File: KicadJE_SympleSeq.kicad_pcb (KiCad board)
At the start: 2 copper layers, 80 x 100 mm, 75 parts, among them J101 CV-Out, J102 Reset + Step, J103 CV-G8_Mod1, J104 CV-G8_Mod2, J105 Clk_Hold, J106 G8-Out, J107 Reset + Step 1-4, J108 Reset + Step 5-8, J109 CV-G8_Base, J201 clk_in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

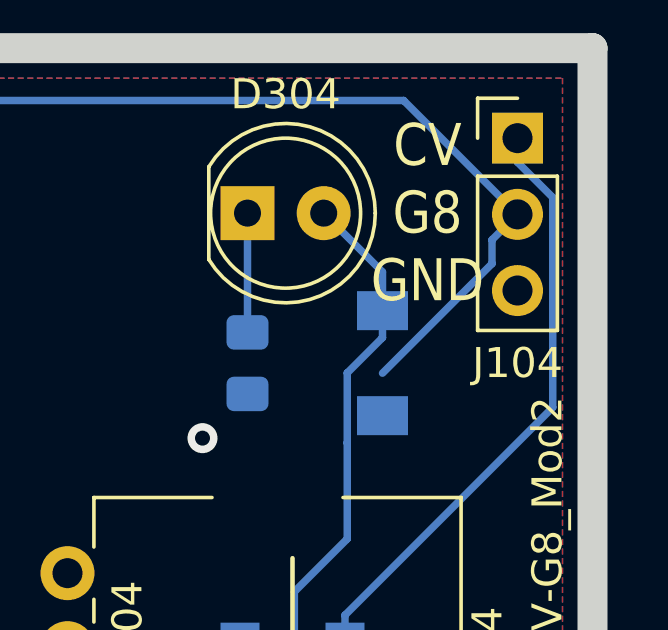
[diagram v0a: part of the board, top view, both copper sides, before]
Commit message: D310 connected
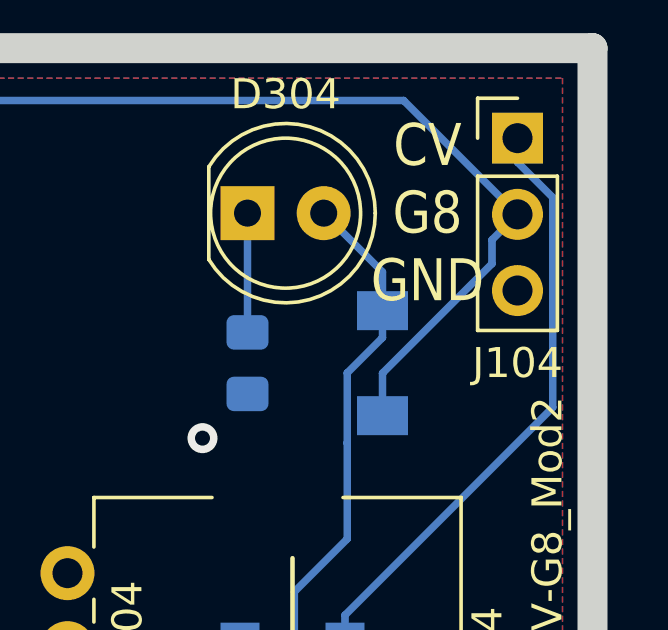
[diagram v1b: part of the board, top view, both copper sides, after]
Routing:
- net G8_M: track 166.9 -> 168.3 mm
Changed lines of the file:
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@@
-(kicad_pcb (version 20171130) (host pcbnew "(5.1.0)-1")
+(kicad_pcb (version 20171130) (host pcbnew "(5.1.5)-3")
   (general
     (thickness 1.6)
     (drawings 22)
-    (tracks 512)
+    (tracks 513)
     (zones 0)
     (modules 75)
@@
   (segment (start 116.369998 102) (end 115.324999 100.955001) (width 0.25) (layer F.Cu) (net 13))
   (segment (start 118.45 102) (end 116.369998 102) (width 0.25) (layer F.Cu) (net 13))
-  (segment (start 176.650001 57.185001) (end 173 60.835002) (width 0.25) (layer B.Cu) (net 14))
-  (segment (start 176.650001 56.389999) (end 176.650001 57.185001) (width 0.25) (layer B.Cu) (net 14))
-  (segment (start 177.5 55.54) (end 176.650001 56.389999) (width 0.25) (layer B.Cu) (net 14))
   (segment (start 113 61.1) (end 113 62) (width 0.25) (layer B.Cu) (net 14))
   (segment (start 114.175001 59.924999) (end 113 61.1) (width 0.25) (layer B.Cu) (net 14))
@@
   (segment (start 177.675001 126.364999) (end 177.675001 123.889999) (width 0.25) (layer F.Cu) (net 14))
   (segment (start 176.5 127.54) (end 177.675001 126.364999) (width 0.25) (layer F.Cu) (net 14))
+  (segment (start 176.650001 56.389999) (end 177.5 55.54) (width 0.25) (layer B.Cu) (net 14))
+  (segment (start 176.650001 57.185001) (end 176.650001 56.389999) (width 0.25) (layer B.Cu) (net 14))
+  (segment (start 173 62.25) (end 173 60.835002) (width 0.25) (layer B.Cu) (net 14))
+  (segment (start 173 60.835002) (end 176.650001 57.185001) (width 0.25) (layer B.Cu) (net 14))
   (segment (start 108.5 55.5) (end 108.5 59.475) (width 0.25) (layer B.Cu) (net 15))
   (segment (start 128.5 56.65) (end 128.5 59.45) (width 0.25) (layer B.Cu) (net 16))

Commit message: Updated PCB rev B
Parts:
- added C101: 100n, AJ:C_0805_AJ, F.Cu at (166.0, 123.2)
- added C102: 100n, AJ:C_0805_AJ, F.Cu at (112.5, 105.0)
- added C103: 100n, AJ:C_0805_AJ, F.Cu at (110.2, 105.0)
- added C104: 100n, AJ:C_0805_AJ, F.Cu at (107.8, 105.0)
- added C105: 100n, AJ:C_0805_AJ, F.Cu at (105.0, 105.0)
- added C106: 100n, AJ:C_0805_AJ, F.Cu at (134.0, 104.5)
- added C107: 100n, AJ:C_0805_AJ, F.Cu at (131.5, 104.5)
- added C108: 100n, AJ:C_0805_AJ, F.Cu at (129.0, 104.5)
- added C109: 100n, AJ:C_0805_AJ, F.Cu at (126.2, 104.5)
- added C207: 47n, AJ:C_0805_AJ, F.Cu at (158.2, 132.5)
- added D101: 5V1 Opt, Diode_SMD:D_MiniMELF, F.Cu at (160.8, 122.5)
- added D102: LL4148, Diode_SMD:D_MiniMELF, F.Cu at (119.2, 104.5)
- added D103: LL4148, Diode_SMD:D_MiniMELF, F.Cu at (138.5, 105.5)
- added D207: On LED, AJ:D_0805_AJ, F.Cu at (172.0, 123.2)
- added D208: 1N4007, Diode_SMD:D_MiniMELF, B.Cu at (168.5, 106.2)
- added D209: 1N4007, Diode_SMD:D_MiniMELF, B.Cu at (168.5, 114.0)
- added J205: Slave clock sel, Connector_PinHeader_2.54mm:PinHeader_1x03_P2.54mm_Vertical, F.Cu at (132.5, 129.0)
- added R212: 10k, AJ:R_0805_AJ, F.Cu at (158.2, 139.2)
- added R213: 10k, AJ:R_0805_AJ, F.Cu at (168.5, 123.2)
- added R214: 10R, AJ:R_0805_AJ, B.Cu at (174.0, 101.5)
- added R215: 10R, AJ:R_0805_AJ, B.Cu at (174.2, 118.8)
- C202, C203, C205: footprint Capacitor_SMD:C_0805_2012Metric_Pad1.15x1.40mm_HandSolder -> AJ:C_0805_AJ
- D201, D202, D203, D204, D205, D206: value 5817 -> 1N4007; footprint LED_SMD:LED_0805_2012Metric -> Diode_SMD:D_MiniMELF
- D301, D302, D303, D304: footprint LED_THT:LED_D5.0mm -> AJ:D_0805_AJ
- J105: value Clk_Hold -> Hold_Rst
- R101, R102, R103, R104, R105, R106, R107, R108, R109, R110, R201, R202, R203, R204, R205, R206, R207, R208, R209, R210, R211: footprint Resistor_SMD:R_0805_2012Metric_Pad1.15x1.40mm_HandSolder -> AJ:R_0805_AJ
- R301, R302, R303, R304: footprint AJ:D_0805_2012Metric_Pad1.15x1.40mm_HandSolder -> AJ:R_0805_AJ
- moved D204 43.0 mm to (105.5, 126.8)
- moved D202 33.1 mm to (140.5, 134.5)
- moved D206 27.4 mm to (140.5, 128.5)
- moved D203 12.4 mm to (160.8, 134.2)
- moved D205 6.75 mm to (160.8, 128.2)
- moved D201 4.47 mm to (105.5, 132.0)
- moved C203 3.91 mm to (133.0, 121.0)
- moved R210 3.91 mm to (129.0, 121.0)
- moved U202 3.91 mm to (127.0, 114.0)
- moved R211 1.13 mm to (120.0, 101.0)
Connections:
- D201 pad 1: +12Vc -> /Clock/clock_out
- D201 pad 2: /Clock/clock_out -> GND
- D202 pad 1: /Clock/clock_out -> /Clock/hold
- D203 pad 1: /Clock/hold -> /Clock/reset
- D204 pad 2: /Clock/hold -> /Clock/clock_out
- D206 pad 1: /Clock/reset -> +12Vc
- D206 pad 2: GND -> /Clock/hold
- J107 pad 1: /Clock/reset -> Net-(D102-Pad2)
- J107 pad 2: /Clock/Q0 -> Net-(C102-Pad2)
- J107 pad 3: /Clock/Q1 -> Net-(C103-Pad2)
- J107 pad 4: /Clock/Q2 -> Net-(C104-Pad2)
- J107 pad 5: /Clock/Q3 -> Net-(C105-Pad2)
- J108 pad 1: /Clock/reset -> Net-(D103-Pad2)
- J108 pad 2: /Clock/Q4 -> Net-(C106-Pad2)
- J108 pad 3: /Clock/Q5 -> Net-(C107-Pad2)
- J108 pad 4: /Clock/Q6 -> Net-(C108-Pad2)
- J108 pad 5: /Clock/Q7 -> Net-(C109-Pad2)
- J203 pad TN: GND -> Net-(J203-PadTN)
- P201 pad 1: -12Vc -> Net-(D207-Pad1)
- P201 pad 10: +12Vc -> Net-(P201-Pad10)
- P201 pad 2: -12Vc -> Net-(D207-Pad1)
- P201 pad 9: +12Vc -> Net-(P201-Pad10)
- R107 pad 1: /Clock/clock_out -> /Clock/hold
- R108 pad 1: /Clock/hold -> /Clock/reset
- R110 pad 2: G8_M -> Net-(C101-Pad1)
- U101 pad 5: G8_M -> Net-(C101-Pad1)
- U202 pad 14: /Clock/clock_out -> /Clock/clk
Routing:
- net /Clock/clock_out: track 75.4 -> 39.5 mm, vias 2 -> 0
- net Net-(C101-Pad1): track 0.00 -> 27.4 mm
- net GND: track 124.0 -> 149.9 mm, vias 38 -> 46
- net +12Vc: track 160.6 -> 184.0 mm, vias 0 -> 1
- net G8_M: track 168.3 -> 147.4 mm
- net /Clock/clk: track 0.00 -> 17.8 mm, vias 0 -> 2
- net Net-(D207-Pad1): track 0.00 -> 15.3 mm
- net /Clock/reset: track 139.7 -> 127.1 mm, vias 2 -> 4
- net /Clock/Q3: track 22.6 -> 31.3 mm
- net Net-(J203-PadTN): track 0.00 -> 6.73 mm
- net Net-(P201-Pad10): track 0.00 -> 5.97 mm
- net -12Vc: track 20.5 -> 26.4 mm, vias 0 -> 1
- net Net-(D102-Pad2): track 0.00 -> 4.97 mm
- net Net-(D103-Pad2): track 0.00 -> 4.60 mm
- net Net-(C102-Pad2): track 0.00 -> 3.64 mm
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
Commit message: PCB rdy for DRC
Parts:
- moved D102 2.30 mm to (117.5, 106.0)
- moved C102 0.50 mm to (113.0, 105.0)
- moved RV201 0.50 mm to (106.0, 111.5)
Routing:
- net /Clock/Q3: track 31.3 -> 32.8 mm
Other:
- board text added: "GND CV"
- board text added: "GND G8"
- board text added: "GND G8 CV"
- board text added: "GND OUT IN"
- board text added: "GND RST HLD"

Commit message: Fix 3mm LED
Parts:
- D301, D302, D303, D304: footprint AJ:D_0805_AJ -> LED_THT:LED_D3.0mm

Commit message: Unconnected fix
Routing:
- net Net-(C102-Pad2): track 3.64 -> 2.78 mm
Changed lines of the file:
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@@
     (thickness 1.6)
     (drawings 27)
-    (tracks 634)
+    (tracks 632)
     (zones 0)
     (modules 96)
@@
   (segment (start 130.77501 109.835466) (end 130.77501 111.604078) (width 0.25) (layer F.Cu) (net 34))
   (segment (start 130.5 109.560456) (end 130.77501 109.835466) (width 0.25) (layer F.Cu) (net 34))
-  (segment (start 112.025 106.025) (end 112 106.025) (width 0.25) (layer F.Cu) (net 35))
-  (segment (start 128.63 111.025) (end 128.63 111.209088) (width 0.25) (layer F.Cu) (net 35) (status 30))
-  (segment (start 128.63 111.209088) (end 127.339088 112.5) (width 0.25) (layer F.Cu) (net 35) (status 10))
-  (segment (start 128.905 110.75) (end 128.63 111.025) (width 0.25) (layer F.Cu) (net 35) (status 30))
+  (segment (start 113 107) (end 113 106.025) (width 0.25) (layer F.Cu) (net 35))
+  (segment (start 128.63 111.025) (end 128.63 111.209088) (width 0.25) (layer F.Cu) (net 35))
+  (segment (start 128.905 110.75) (end 128.63 111.025) (width 0.25) (layer F.Cu) (net 35))
+  (segment (start 128.63 111.209088) (end 127.339088 112.5) (width 0.25) (layer F.Cu) (net 35))
   (segment (start 127.339088 112.5) (end 118.5 112.5) (width 0.25) (layer F.Cu) (net 35))
-  (segment (start 118.5 112.5) (end 112.025 106.025) (width 0.25) (layer F.Cu) (net 35))
+  (segment (start 118.5 112.5) (end 113 107) (width 0.25) (layer F.Cu) (net 35))
   (segment (start 129.82929 111.09571) (end 129.82929 111.36212) (width 0.25) (layer F.Cu) (net 36))
   (segment (start 128.241401 112.950009) (end 117.075009 112.950009) (width 0.25) (layer F.Cu) (net 36))
@@
   (segment (start 156.874999 117.974999) (end 156.874999 114.75) (width 0.25) (layer F.Cu) (net 51))
   (segment (start 159.65 120.75) (end 156.874999 117.974999) (width 0.25) (layer F.Cu) (net 51))
-  (segment (start 112.5 103.975) (end 112 103.975) (width 0.25) (layer F.Cu) (net 52) (status 10))
-  (segment (start 112.75 103.725) (end 112.5 103.975) (width 0.25) (layer F.Cu) (net 52) (status 30))
   (segment (start 112.784999 100.955001) (end 112.75 100.99) (width 0.25) (layer F.Cu) (net 52) (status 30))
   (segment (start 112.75 100.99) (end 112.75 103.725) (width 0.25) (layer F.Cu) (net 52) (status 30))

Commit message: Fix few things for RevB (2)
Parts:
- moved R203 2.50 mm to (110.0, 128.1)
- moved R204 2.50 mm to (110.0, 132.5)
- moved J201 0.50 mm to (114.5, 144.0)
- moved J202 0.50 mm to (134.5, 144.0)
- moved J203 0.50 mm to (154.5, 144.0)
- moved J204 0.50 mm to (174.5, 144.0)
- moved C106 0.25 mm to (134.0, 104.8)
- moved C107 0.25 mm to (131.5, 104.7)
- moved C108 0.25 mm to (129.0, 104.8)
- moved C109 0.25 mm to (126.2, 104.8)
- moved D204 0.25 mm to (105.5, 126.5)
- moved R205 0.25 mm to (130.0, 132.8)
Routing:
- net GND: track 149.9 -> 147.0 mm
- net Net-(J201-PadT): track 14.1 -> 16.6 mm
- net /Clock/clock_out: track 39.5 -> 37.2 mm
- net /Clock/Q7: track 14.7 -> 14.0 mm

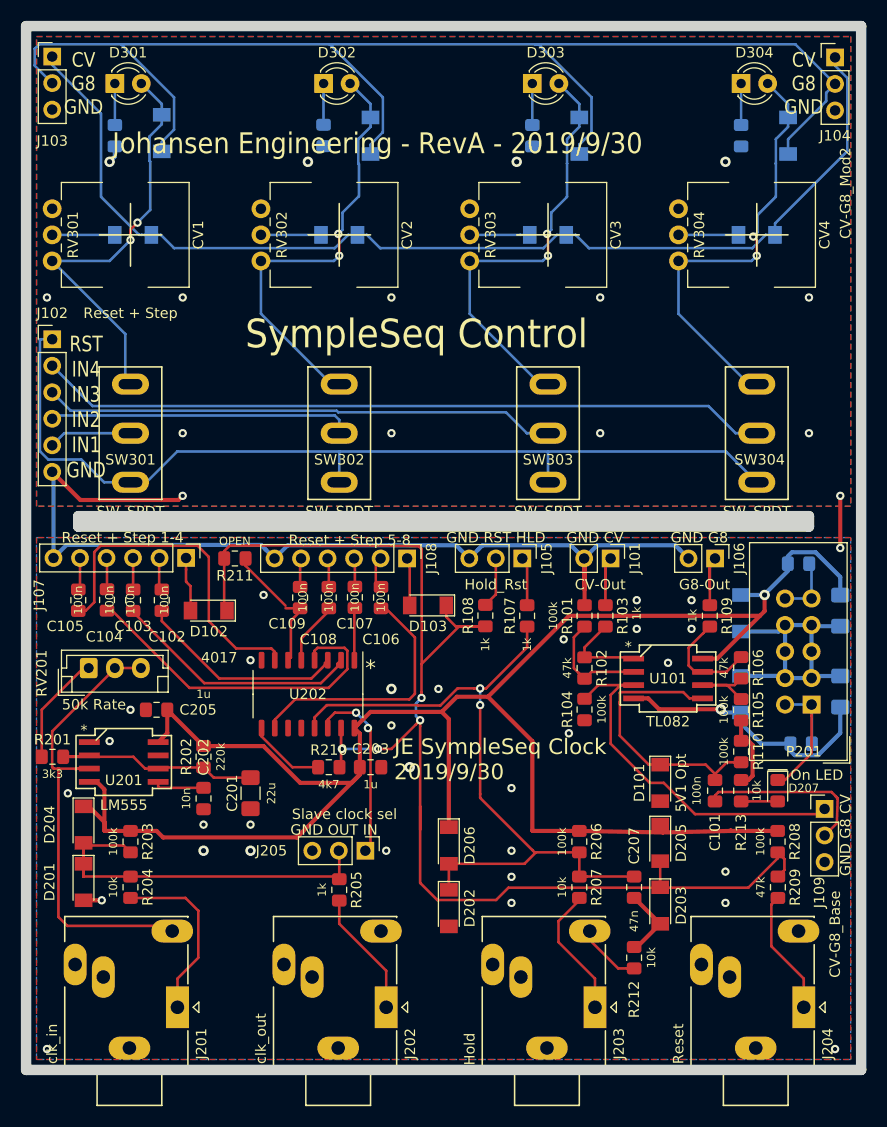
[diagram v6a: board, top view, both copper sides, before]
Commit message: RevB2
fix Jack a bit further to the front
labeling
Minor adj to fix courtyard overlaps
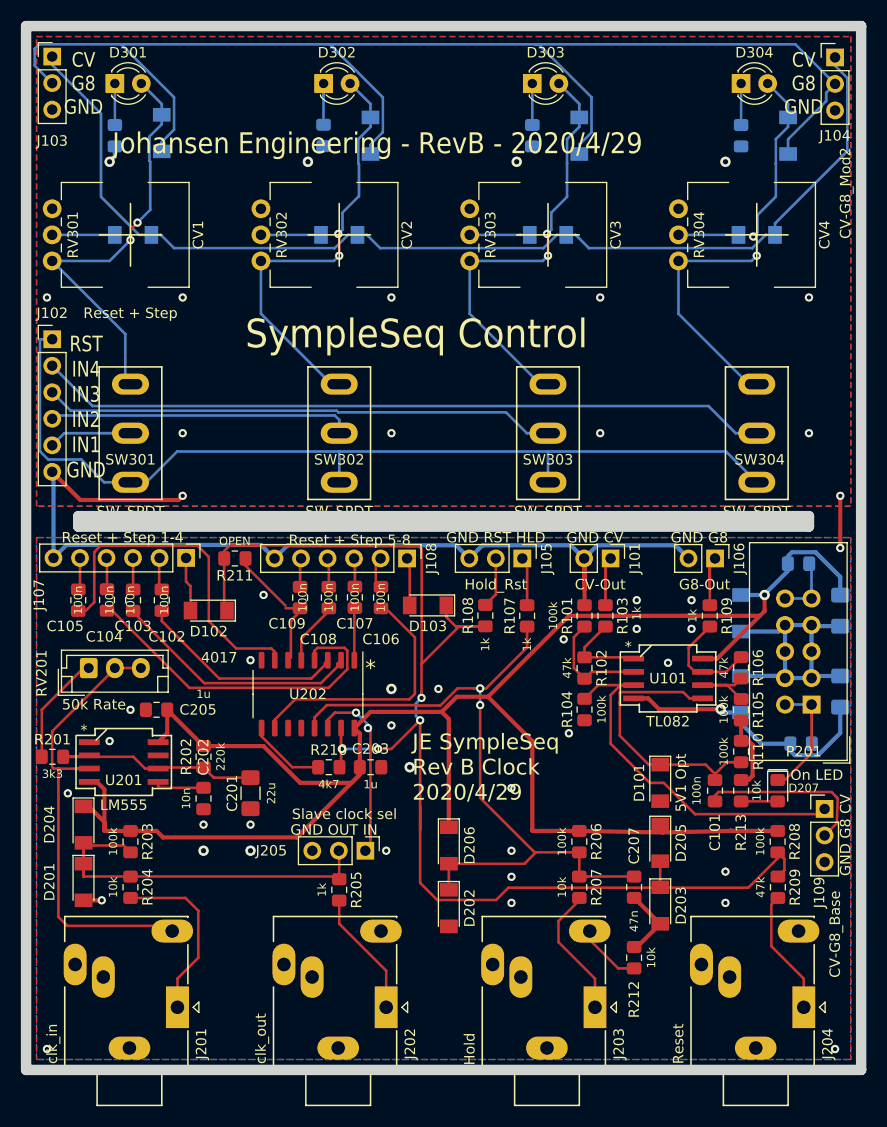
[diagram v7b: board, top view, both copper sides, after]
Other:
- board text added: "JE SympleSeq Rev B Clock 2020/4/29"
- board text added: "Johansen Engineering - RevB - 2020/4/29"
- board text removed: "JE SympleSeq Clock 2019/9/30"
- board text removed: "Johansen Engineering - RevA - 2019/9/30"
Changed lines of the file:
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@@
   (general
     (thickness 1.6)
-    (drawings 27)
+    (drawings 29)
     (tracks 628)
     (zones 0)
@@
     )
   )
+  (gr_text "SympleSeq Control " (at 158.95 79.5) (layer B.SilkS)
+    (effects (font (size 2.75 2.5) (thickness 0.45)) (justify left mirror))
+  )
+  (gr_text "Johansen Engineering - RevB - 2020/4/29" (at 170.5 61.25) (layer B.SilkS)
+    (effects (font (size 2 1.8) (thickness 0.45)) (justify left mirror))
+  )
   (gr_text "GND G8 CV" (at 178.5 127.5 90) (layer F.SilkS)
     (effects (font (size 1 1) (thickness 0.1)))
@@
     (effects (font (size 1.5 1.2) (thickness 0.3)) (justify mirror))
   )
-  (gr_text "Johansen Engineering - RevA - 2019/9/30" (at 108.25 61.25) (layer F.SilkS)
+  (gr_text "Johansen Engineering - RevB - 2020/4/29" (at 108.25 61.25) (layer F.SilkS)
     (effects (font (size 2 1.8) (thickness 0.45)) (justify left))
   )
@@
   (gr_line (start 130 50.5) (end 130 150) (layer Dwgs.User) (width 0.15))
   (gr_line (start 110 50.5) (end 110 150) (layer Dwgs.User) (width 0.15))
-  (gr_text "JE SympleSeq Clock\n2019/9/30" (at 135.25 120.25) (layer F.SilkS)
+  (gr_text "JE SympleSeq \nRev B Clock\n2020/4/29" (at 137 121) (layer F.SilkS)
     (effects (font (size 1.5 1.5) (thickness 0.375)) (justify left))
   )
